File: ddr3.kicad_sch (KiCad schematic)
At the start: 27 parts, among them U11 LIFCL-40-9BG256C, U12 MT41K128M16JT-125_K

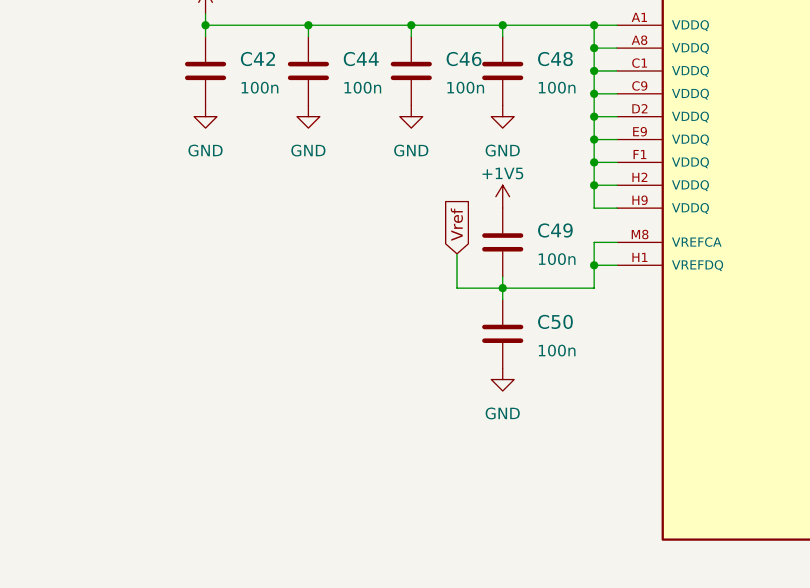
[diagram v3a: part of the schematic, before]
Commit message: Routed rest of low speed signals
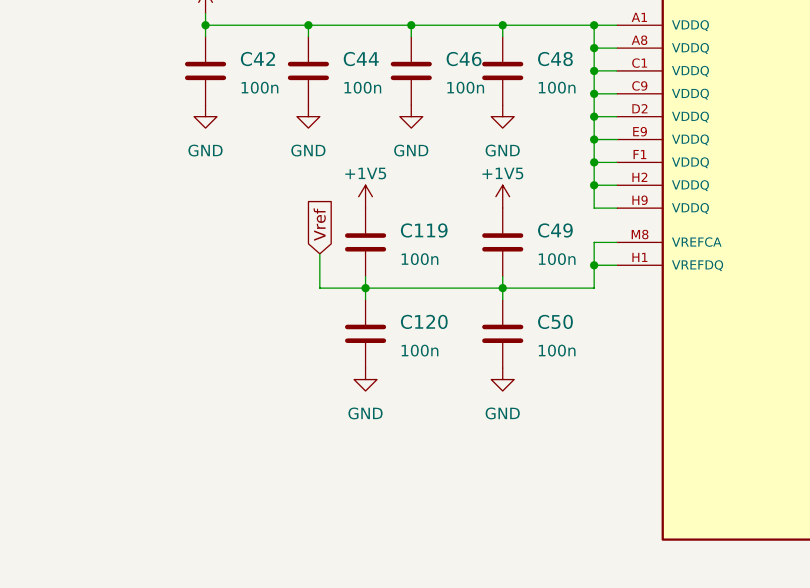
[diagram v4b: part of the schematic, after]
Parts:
- added C119, C120: C_100n_0402, crosslink-nx-video-converter-footprints:0402-cap, symbol crosslink-nx-video-converter:C_100n_0402
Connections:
- net +1V5: now also C119.1
- net GND: now also C120.2
- net Vref: now also C119.2, C120.1
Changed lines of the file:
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@@
   (junction (at 384.81 74.93) (diameter 0) (color 0 0 0 0)
   )
+  (junction (at 313.69 107.95) (diameter 0) (color 0 0 0 0)
+  )
   (junction (at 226.06 250.19) (diameter 0) (color 0 0 0 0)
   )
@@
     (stroke (width 0) (type default) (color 0 0 0 0))
   )
+  (wire (pts (xy 308.61 107.95) (xy 313.69 107.95))
+    (stroke (width 0) (type default) (color 0 0 0 0))
+  )
   (wire (pts (xy 203.2 95.25) (xy 214.63 95.25))
     (stroke (width 0) (type default) (color 0 0 0 0))
@@
     (stroke (width 0) (type default) (color 0 0 0 0))
   )
+  (wire (pts (xy 313.69 107.95) (xy 313.69 109.22))
+    (stroke (width 0) (type default) (color 0 0 0 0))
+  )
   (wire (pts (xy 95.25 191.77) (xy 113.03 191.77))
     (stroke (width 0) (type default) (color 0 0 0 0))
@@
     (stroke (width 0) (type default) (color 0 0 0 0))
   )
+  (wire (pts (xy 313.69 106.68) (xy 313.69 107.95))
+    (stroke (width 0) (type default) (color 0 0 0 0))
+  )
   (wire (pts (xy 190.5 87.63) (xy 190.5 88.9))
     (stroke (width 0) (type default) (color 0 0 0 0))
@@
     (stroke (width 0) (type default) (color 0 0 0 0))
   )
-  (wire (pts (xy 323.85 107.95) (xy 328.93 107.95))
-    (stroke (width 0) (type default) (color 0 0 0 0))
-  )
   (wire (pts (xy 218.44 247.65) (xy 226.06 247.65))
     (stroke (width 0) (type default) (color 0 0 0 0))
@@
     (stroke (width 0) (type default) (color 0 0 0 0))
   )
-  (wire (pts (xy 323.85 104.14) (xy 323.85 107.95))
+  (wire (pts (xy 308.61 104.14) (xy 308.61 107.95))
     (stroke (width 0) (type default) (color 0 0 0 0))
   )
@@
   )
   (wire (pts (xy 95.25 242.57) (xy 97.79 242.57))
+    (stroke (width 0) (type default) (color 0 0 0 0))
+  )
+  (wire (pts (xy 313.69 107.95) (xy 328.93 107.95))
     (stroke (width 0) (type default) (color 0 0 0 0))
   )
@@
     )
   )
-  (global_label "Vref" (shape input) (at 323.85 104.14 90) (fields_autoplaced)
+  (global_label "Vref" (shape input) (at 308.61 104.14 90) (fields_autoplaced)
     (effects (font (size 1.27 1.27)) (justify left))
-    (property "Intersheet References" "${INTERSHEET_REFS}" (id 0) (at 323.7706 98.0379 90)
+    (property "Intersheet References" "${INTERSHEET_REFS}" (id 0) (at 308.5306 98.0379 90)
       (effects (font (size 1.27 1.27)) (justify left) hide)
     )
@@
     )
     (property "Datasheet" "" (id 3) (at 295.91 63.5 0)
+      (effects (font (size 1.27 1.27)) hide)
+    )
+    (pin "1")
+  )
+  (symbol (lib_id "crosslink-nx-video-converter:GND") (at 313.69 116.84 0) (unit 1)
+    (in_bom yes) (on_board yes) (fields_autoplaced)
+    (property "Reference" "#PWR0262" (id 0) (at 313.69 123.19 0)
+      (effects (font (size 1.27 1.27)) hide)
+    )
+    (property "Value" "GND" (id 1) (at 313.69 121.92 0))
+    (property "Footprint" "crosslink-nx-video-converter-footprints:" (id 2) (at 313.69 116.84 0)
+      (effects (font (size 1.27 1.27)) hide)
+    )
+    (property "Datasheet" "" (id 3) (at 313.69 116.84 0)
       (effects (font (size 1.27 1.27)) hide)
     )
@@
     (pin "1")
   )
+  (symbol (lib_id "crosslink-nx-video-converter:+1V5") (at 313.69 99.06 0) (unit 1)
+    (in_bom yes) (on_board yes)
+    (property "Reference" "#PWR0261" (id 0) (at 313.69 102.87 0)
+      (effects (font (size 1.27 1.27)) hide)
+    )
+    (property "Value" "+1V5" (id 1) (at 313.69 95.25 0))
+    (property "Footprint" "crosslink-nx-video-converter-footprints:" (id 2) (at 313.69 99.06 0)
+      (effects (font (size 1.27 1.27)) hide)
+    )
+    (property "Datasheet" "" (id 3) (at 313.69 99.06 0)
+      (effects (font (size 1.27 1.27)) hide)
+    )
+    (pin "1")
+  )
   (symbol (lib_id "crosslink-nx-video-converter:C_100n_0402") (at 295.91 59.69 0) (unit 1)
     (in_bom yes) (on_board yes) (fields_autoplaced)
@@
     (pin "1")
   )
+  (symbol (lib_id "crosslink-nx-video-converter:C_100n_0402") (at 313.69 113.03 0) (unit 1)
+    (in_bom yes) (on_board yes) (fields_autoplaced)
+    (property "Reference" "C120" (id 0) (at 317.5 111.76 0)
+      (effects (font (size 1.524 1.524)) (justify left))
+    )
+    (property "Value" "C_100n_0402" (id 1) (at 313.69 116.84 0)
+      (effects (font (size 1.524 1.524)) hide)
+    )
+    (property "Footprint" "crosslink-nx-video-converter-footprints:0402-cap" (id 2) (at 318.77 107.95 0)
+      (effects (font (size 1.524 1.524)) (justify left) hide)
+    )
+    (property "Datasheet" "" (id 3) (at 313.69 113.03 0)
+      (effects (font (size 1.27 1.27)) hide)
+    )
+    (property "Manufacturer" "Murata" (id 4) (at 318.77 102.87 0)
+      (effects (font (size 1.524 1.524)) (justify left) hide)
+    )
+    (property "MPN" "GRM155R61H104KE14D" (id 5) (at 318.77 105.41 0)
+      (effects (font (size 1.524 1.524)) (justify left) hide)
+    )
+    (property "Val" "100n" (id 6) (at 317.5 114.9349 0)
+      (effects (font (size 1.27 1.27)) (justify left))
+    )
+    (pin "1")
+    (pin "2")
+  )
   (symbol (lib_id "crosslink-nx-video-converter:C_100n_0402") (at 134.62 53.34 0) (mirror y) (unit 1)
     (in_bom yes) (on_board yes)
@@
     (pin "1")
     (pin "2")
+  )
+  (symbol (lib_id "crosslink-nx-video-converter:C_100n_0402") (at 313.69 102.87 0) (unit 1)
+    (in_bom yes) (on_board yes) (fields_autoplaced)
+    (property "Reference" "C119" (id 0) (at 317.5 101.6 0)
+      (effects (font (size 1.524 1.524)) (justify left))
+    )
+    (property "Value" "C_100n_0402" (id 1) (at 313.69 106.68 0)
+      (effects (font (size 1.524 1.524)) hide)
+    )
+    (property "Footprint" "crosslink-nx-video-converter-footprints:0402-cap" (id 2) (at 318.77 97.79 0)
+      (effects (font (size 1.524 1.524)) (justify left) hide)
+    )
+    (property "Datasheet" "" (id 3) (at 313.69 102.87 0)
+      (effects (font (size 1.27 1.27)) hide)
+    )
+    (property "Manufacturer" "Murata" (id 4) (at 318.77 92.71 0)
+      (effects (font (size 1.524 1.524)) (justify left) hide)
+    )
+    (property "MPN" "GRM155R61H104KE14D" (id 5) (at 318.77 95.25 0)
+      (effects (font (size 1.524 1.524)) (justify left) hide)
+    )
+    (property "Val" "100n" (id 6) (at 317.5 104.7749 0)
+      (effects (font (size 1.27 1.27)) (justify left))
+    )
+    (pin "1")
+    (pin "2")

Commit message: Created loclib
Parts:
- U11: footprint antmicro-footprints:BGA-256_16x16_14.0x14.0mm -> crosslink-nx-video-converter-footprints:BGA-256_16x16_14.0x14.0mm; symbol antmicroBGAchips:LIFCL-40-9BG256C -> crosslink-nx-video-converter:LIFCL-40-9BG256C
- U12: footprint antmicro-footprints:BGA80P96C6X16_800X1400X110 -> crosslink-nx-video-converter-footprints:BGA80P96C6X16_800X1400X110; symbol antmicroMemory:MT41K128M16JT-125_K -> crosslink-nx-video-converter:MT41K128M16JT-125_K
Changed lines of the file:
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@@
     )
     (property "Value" "GND" (id 1) (at 123.19 73.66 0))
-    (property "Footprint" "crosslink-nx-video-converter-footprints:" (id 2) (at 123.19 68.58 0)
+    (property "Footprint" "" (id 2) (at 123.19 68.58 0)
       (effects (font (size 1.27 1.27)) hide)
     )
@@
     )
     (property "Value" "GND" (id 1) (at 307.34 68.58 0))
-    (property "Footprint" "crosslink-nx-video-converter-footprints:" (id 2) (at 307.34 63.5 0)
+    (property "Footprint" "" (id 2) (at 307.34 63.5 0)
       (effects (font (size 1.27 1.27)) hide)
     )
@@
     )
     (property "Value" "+1V5" (id 1) (at 125.73 168.91 0))
-    (property "Footprint" "crosslink-nx-video-converter-footprints:" (id 2) (at 125.73 172.72 0)
+    (property "Footprint" "" (id 2) (at 125.73 172.72 0)
       (effects (font (size 1.27 1.27)) hide)
     )
@@
     )
     (property "Value" "GND" (id 1) (at 295.91 68.58 0))
-    (property "Footprint" "crosslink-nx-video-converter-footprints:" (id 2) (at 295.91 63.5 0)
+    (property "Footprint" "" (id 2) (at 295.91 63.5 0)
       (effects (font (size 1.27 1.27)) hide)
     )
@@
     )
     (property "Value" "GND" (id 1) (at 313.69 121.92 0))
-    (property "Footprint" "crosslink-nx-video-converter-footprints:" (id 2) (at 313.69 116.84 0)
+    (property "Footprint" "" (id 2) (at 313.69 116.84 0)
       (effects (font (size 1.27 1.27)) hide)
     )
@@
     )
     (property "Value" "GND" (id 1) (at 328.93 92.71 0))
-    (property "Footprint" "crosslink-nx-video-converter-footprints:" (id 2) (at 328.93 87.63 0)
+    (property "Footprint" "" (id 2) (at 328.93 87.63 0)
       (effects (font (size 1.27 1.27)) hide)
     )
@@
     )
     (property "Value" "GND" (id 1) (at 328.93 121.92 0))
-    (property "Footprint" "crosslink-nx-video-converter-footprints:" (id 2) (at 328.93 116.84 0)
+    (property "Footprint" "" (id 2) (at 328.93 116.84 0)
       (effects (font (size 1.27 1.27)) hide)
     )
@@
     )
     (property "Value" "GND" (id 1) (at 295.91 92.71 0))
-    (property "Footprint" "crosslink-nx-video-converter-footprints:" (id 2) (at 295.91 87.63 0)
+    (property "Footprint" "" (id 2) (at 295.91 87.63 0)
       (effects (font (size 1.27 1.27)) hide)
     )
@@
     )
     (property "Value" "+1V5" (id 1) (at 313.69 95.25 0))
-    (property "Footprint" "crosslink-nx-video-converter-footprints:" (id 2) (at 313.69 99.06 0)
+    (property "Footprint" "" (id 2) (at 313.69 99.06 0)
       (effects (font (size 1.27 1.27)) hide)
     )
@@
     (pin "2")
   )
-  (symbol (lib_id "antmicroMemory:MT41K128M16JT-125_K") (at 219.71 52.07 0) (unit 1)
+  (symbol (lib_id "crosslink-nx-video-converter:MT41K128M16JT-125_K") (at 219.71 52.07 0) (unit 1)
     (in_bom yes) (on_board yes) (fields_autoplaced)
     (property "Reference" "U12" (id 0) (at 234.95 48.26 0))
     (property "Value" "MT41K128M16JT-125_K" (id 1) (at 234.95 50.8 0))
-    (property "Footprint" "antmicro-footprints:BGA80P96C6X16_800X1400X110" (id 2) (at 285.75 92.71 0)
+    (property "Footprint" "crosslink-nx-video-converter-footprints:BGA80P96C6X16_800X1400X110" (id 2) (at 285.75 92.71 0)
       (effects (font (size 1.27 1.27)) (justify left bottom) hide)
     )
@@
     )
     (property "Value" "GND" (id 1) (at 318.77 68.58 0))
-    (property "Footprint" "crosslink-nx-video-converter-footprints:" (id 2) (at 318.77 63.5 0)
+    (property "Footprint" "" (id 2) (at 318.77 63.5 0)
       (effects (font (size 1.27 1.27)) hide)
     )
@@
     )
     (property "Value" "GND" (id 1) (at 256.54 127 0))
-    (property "Footprint" "crosslink-nx-video-converter-footprints:" (id 2) (at 256.54 121.92 0)
+    (property "Footprint" "" (id 2) (at 256.54 121.92 0)
       (effects (font (size 1.27 1.27)) hide)
     )
@@
     )
     (property "Value" "GND" (id 1) (at 388.62 88.9 0))
-    (property "Footprint" "crosslink-nx-video-converter-footprints:" (id 2) (at 388.62 83.82 0)
+    (property "Footprint" "" (id 2) (at 388.62 83.82 0)
       (effects (font (size 1.27 1.27)) hide)
     )
@@
     )
     (property "Value" "GND" (id 1) (at 140.97 190.5 0))
-    (property "Footprint" "crosslink-nx-video-converter-footprints:" (id 2) (at 140.97 185.42 0)
+    (property "Footprint" "" (id 2) (at 140.97 185.42 0)
       (effects (font (size 1.27 1.27)) hide)
     )
@@
     )
     (property "Value" "+1V5" (id 1) (at 140.97 163.83 0))
-    (property "Footprint" "crosslink-nx-video-converter-footprints:" (id 2) (at 140.97 167.64 0)
+    (property "Footprint" "" (id 2) (at 140.97 167.64 0)
       (effects (font (size 1.27 1.27)) hide)
     )
@@
     (pin "1")
   )
-  (symbol (lib_id "antmicroBGAchips:LIFCL-40-9BG256C") (at 73.66 93.98 0) (unit 4)
+  (symbol (lib_id "crosslink-nx-video-converter:LIFCL-40-9BG256C") (at 73.66 93.98 0) (unit 4)
     (in_bom yes) (on_board yes) (fields_autoplaced)
     (property "Reference" "U11" (id 0) (at 72.39 48.26 0))
     (property "Value" "LIFCL-40-9BG256C" (id 1) (at 72.39 50.8 0))
-    (property "Footprint" "antmicro-footprints:BGA-256_16x16_14.0x14.0mm" (id 2) (at 75.565 236.855 0)
+    (property "Footprint" "crosslink-nx-video-converter-footprints:BGA-256_16x16_14.0x14.0mm" (id 2) (at 75.565 236.855 0)
       (effects (font (size 1.27 1.27)) hide)
     )
@@
     )
     (property "Value" "+1V5" (id 1) (at 134.62 45.72 0))
-    (property "Footprint" "crosslink-nx-video-converter-footprints:" (id 2) (at 134.62 49.53 0)
+    (property "Footprint" "" (id 2) (at 134.62 49.53 0)
       (effects (font (size 1.27 1.27)) hide)
     )
@@
     )
     (property "Value" "+1V5" (id 1) (at 328.93 95.25 0))
-    (property "Footprint" "crosslink-nx-video-converter-footprints:" (id 2) (at 328.93 99.06 0)
+    (property "Footprint" "" (id 2) (at 328.93 99.06 0)
       (effects (font (size 1.27 1.27)) hide)
     )
@@
     )
     (property "Value" "GND" (id 1) (at 118.11 190.5 0))
-    (property "Footprint" "crosslink-nx-video-converter-footprints:" (id 2) (at 118.11 185.42 0)
+    (property "Footprint" "" (id 2) (at 118.11 185.42 0)
       (effects (font (size 1.27 1.27)) hide)
     )
@@
     )
     (property "Value" "GND" (id 1) (at 388.62 113.03 0))
-    (property "Footprint" "crosslink-nx-video-converter-footprints:" (id 2) (at 388.62 107.95 0)
+    (property "Footprint" "" (id 2) (at 388.62 107.95 0)
       (effects (font (size 1.27 1.27)) hide)
     )
@@
     )
     (property "Value" "GND" (id 1) (at 97.79 144.78 0))
-    (property "Footprint" "crosslink-nx-video-converter-footprints:" (id 2) (at 97.79 140.97 0)
+    (property "Footprint" "" (id 2) (at 97.79 140.97 0)
       (effects (font (size 1.27 1.27)) hide)
     )
@@
     )
     (property "Value" "GND" (id 1) (at 307.34 92.71 0))
-    (property "Footprint" "crosslink-nx-video-converter-footprints:" (id 2) (at 307.34 87.63 0)
+    (property "Footprint" "" (id 2) (at 307.34 87.63 0)
       (effects (font (size 1.27 1.27)) hide)
     )
@@
     )
     (property "Value" "GND" (id 1) (at 125.73 190.5 0))
-    (property "Footprint" "crosslink-nx-video-converter-footprints:" (id 2) (at 125.73 185.42 0)
+    (property "Footprint" "" (id 2) (at 125.73 185.42 0)
       (effects (font (size 1.27 1.27)) hide)
     )
@@
     )
     (property "Value" "GND" (id 1) (at 328.93 68.58 0))
-    (property "Footprint" "crosslink-nx-video-converter-footprints:" (id 2) (at 328.93 63.5 0)
+    (property "Footprint" "" (id 2) (at 328.93 63.5 0)
       (effects (font (size 1.27 1.27)) hide)
     )
@@
     )
     (property "Value" "GND" (id 1) (at 318.77 92.71 0))
-    (property "Footprint" "crosslink-nx-video-converter-footprints:" (id 2) (at 318.77 87.63 0)
+    (property "Footprint" "" (id 2) (at 318.77 87.63 0)
       (effects (font (size 1.27 1.27)) hide)
     )
@@
     )
     (property "Value" "GND" (id 1) (at 97.79 261.62 0))
-    (property "Footprint" "crosslink-nx-video-converter-footprints:" (id 2) (at 97.79 257.81 0)
+    (property "Footprint" "" (id 2) (at 97.79 257.81 0)
       (effects (font (size 1.27 1.27)) hide)
     )
@@
     )
     (property "Value" "+1V5" (id 1) (at 295.91 73.66 0))
-    (property "Footprint" "crosslink-nx-video-converter-footprints:" (id 2) (at 295.91 77.47 0)
+    (property "Footprint" "" (id 2) (at 295.91 77.47 0)
       (effects (font (size 1.27 1.27)) hide)
     )
@@
     (pin "1")
   )
-  (symbol (lib_id "antmicroMemory:MT41K128M16JT-125_K") (at 346.71 52.07 0) (unit 2)
+  (symbol (lib_id "crosslink-nx-video-converter:MT41K128M16JT-125_K") (at 346.71 52.07 0) (unit 2)
     (in_bom yes) (on_board yes) (fields_autoplaced)
     (property "Reference" "U12" (id 0) (at 361.95 48.26 0))
     (property "Value" "MT41K128M16JT-125_K" (id 1) (at 361.95 50.8 0))
-    (property "Footprint" "antmicro-footprints:BGA80P96C6X16_800X1400X110" (id 2) (at 412.75 92.71 0)
+    (property "Footprint" "crosslink-nx-video-converter-footprints:BGA80P96C6X16_800X1400X110" (id 2) (at 412.75 92.71 0)
       (effects (font (size 1.27 1.27)) (justify left bottom) hide)
     )
@@
     )
     (property "Value" "GND" (id 1) (at 134.62 72.39 0))
-    (property "Footprint" "crosslink-nx-video-converter-footprints:" (id 2) (at 134.62 67.31 0)
+    (property "Footprint" "" (id 2) (at 134.62 67.31 0)
       (effects (font (size 1.27 1.27)) hide)
     )
@@
     )
     (property "Value" "+1V5" (id 1) (at 295.91 49.53 0))
-    (property "Footprint" "crosslink-nx-video-converter-footprints:" (id 2) (at 295.91 53.34 0)
+    (property "Footprint" "" (id 2) (at 295.91 53.34 0)
       (effects (font (size 1.27 1.27)) hide)
     )
@@
     )
     (property "Value" "+1V5" (id 1) (at 123.19 50.8 0))
-    (property "Footprint" "crosslink-nx-video-converter-footprints:" (id 2) (at 123.19 54.61 0)
-      (effects (font (size 1.27 1.27)) hide)
-    )
+    (property "Footprint" "" (id 2) (at 123.19 54.61 0)
+      (effects (font (size 1.27 1.27)) hide)
+    )

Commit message: Added revision and title to the schematic sheets
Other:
- title: (none) -> CrossLink-NX Video Converter
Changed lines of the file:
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@@
 (kicad_sch (version 20211123) (generator eeschema)
   (paper "A3")
+  (title_block
+    (title "CrossLink-NX Video Converter")
+    (date "2022-10-27")
+    (rev "1.0.0")
+    (comment 1 "www.antmicro.com")
+    (comment 2 "Antmicro Ltd.")
+  )
   (junction (at 339.09 78.74) (diameter 0) (color 0 0 0 0)
   )
